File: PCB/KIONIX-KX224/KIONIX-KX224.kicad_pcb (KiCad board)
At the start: 2 copper layers, 4 parts, among them J1 Conn_02x03_Odd_Even

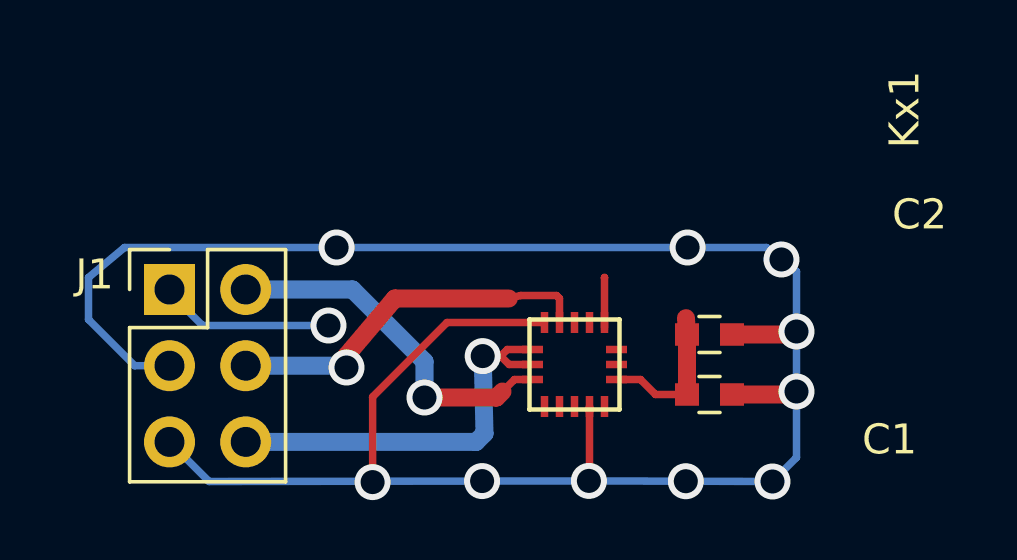
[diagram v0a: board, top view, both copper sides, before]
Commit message: PCB - update KX224
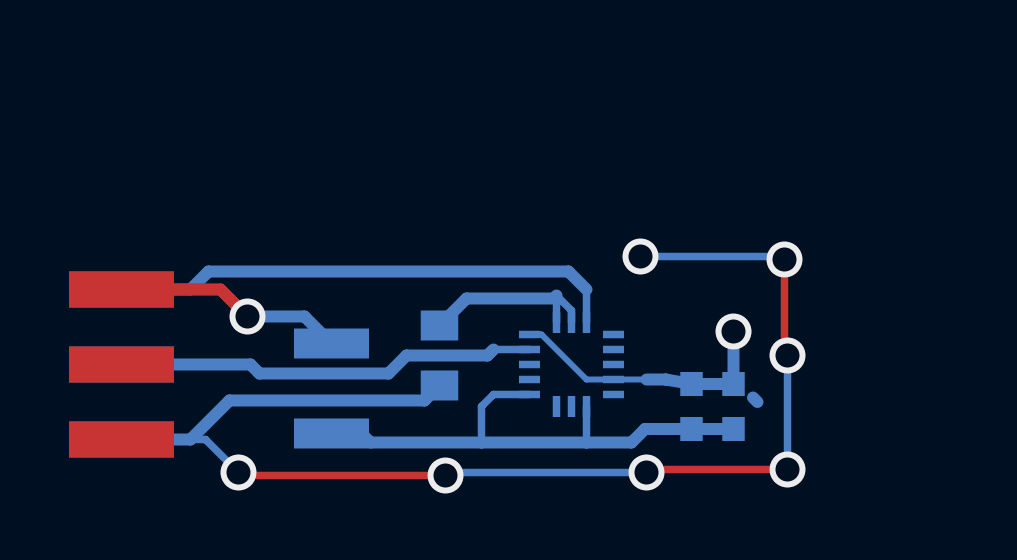
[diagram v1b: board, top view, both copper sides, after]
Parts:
- added J2, J5: Conn_01x01, DIY_KICAD_FOOTPRINT_LIBRARY:pastilles_CMS_rect_1,2_3,5, F.Cu at (128.9, 94.5)
- added J3, J6: Conn_01x01, DIY_KICAD_FOOTPRINT_LIBRARY:pastilles_CMS_rect_1,2_3,5, F.Cu at (128.9, 97.0)
- added J4: Conn_01x01, DIY_KICAD_FOOTPRINT_LIBRARY:pastilles_CMS_rect_1,2_3,5, F.Cu at (128.9, 92.0)
- added JP1: Jumper, Capacitors_SMD:C_0805, B.Cu at (139.5, 94.2)
- added JP2: Jumper, Capacitors_SMD:C_1210, B.Cu at (135.9, 95.3)
- C1, C2, Kx1: moved to B.Cu
- J1: value Conn_02x03_Odd_Even -> Conn_01x01; footprint Pin_Headers:Pin_Header_Straight_2x03_Pitch2.54mm -> DIY_KICAD_FOOTPRINT_LIBRARY:pastilles_CMS_rect_1,2_3,5
- moved C2 2.47 mm to (147.9, 95.9), turned to 90 degrees
- moved J1 1.60 mm to (128.9, 92.0)
- moved C1 0.89 mm to (149.3, 95.9), turned to 90 degrees
- moved Kx1 0.10 mm to (143.9, 94.5), turned to 0 degrees
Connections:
- J1 pad 1: /VDD -> Net-(J1-Pad1)
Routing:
- net GNDREF: track 73.8 -> 9.28 mm, vias 10 -> 1
- net Net-(J6-Pad1): track 0.00 -> 46.1 mm, vias 0 -> 7
- net Net-(J1-Pad1): track 0.00 -> 7.75 mm, vias 0 -> 1
- net /Miso/Mosi: track 13.6 -> 6.38 mm, vias 1 -> 0
- net /CS/SCL: track 12.3 -> 18.6 mm, vias 1 -> 0
- net /VDD: track 12.7 -> 18.6 mm, vias 1 -> 0
- net /SCLK: track 12.6 -> 14.1 mm, vias 1 -> 0

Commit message: PCB - Kionix v 1.5, ready to print
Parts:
- added JP3: Jumper, Capacitors_SMD:C_1210, B.Cu at (140.1, 93.1)
- moved JP1 2.73 mm to (137.0, 95.3)
- moved C1 2.40 mm to (148.8, 93.5), turned to 0 degrees
- moved JP2 2.06 mm to (133.8, 95.5)
- moved C2 1.77 mm to (149.6, 96.5)
- moved Kx1 0.92 mm to (144.5, 95.2)
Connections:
- Kx1 pad 10: (no net) -> Net-(Kx1-Pad10)
- Kx1 pad 11: (no net) -> Net-(Kx1-Pad11)
- Kx1 pad 13: (no net) -> Net-(Kx1-Pad13)
- Kx1 pad 15: (no net) -> Net-(Kx1-Pad15)
- Kx1 pad 16: (no net) -> Net-(Kx1-Pad16)
- Kx1 pad 2: (no net) -> Net-(Kx1-Pad2)
- Kx1 pad 3: (no net) -> Net-(Kx1-Pad3)
- Kx1 pad 5: GNDREF -> Net-(JP3-Pad2)
- Kx1 pad 9: (no net) -> Net-(Kx1-Pad9)
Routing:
- net GNDREF: track 9.28 -> 69.3 mm, vias 1 -> 9
- net Net-(J6-Pad1): track 46.1 -> 8.80 mm, vias 7 -> 0
- net /VDD: track 18.6 -> 25.1 mm
- net Net-(JP3-Pad2): track 0.00 -> 3.19 mm
- net /Miso/Mosi: track 6.38 -> 9.19 mm
- net /SCLK: track 14.1 -> 16.2 mm
- net Net-(J1-Pad1): track 7.75 -> 9.46 mm
- net /CS/SCL: track 18.6 -> 19.6 mm
- added copper zone on B.Cu, net GNDREF
- added copper zone on F.Cu, net GNDREF

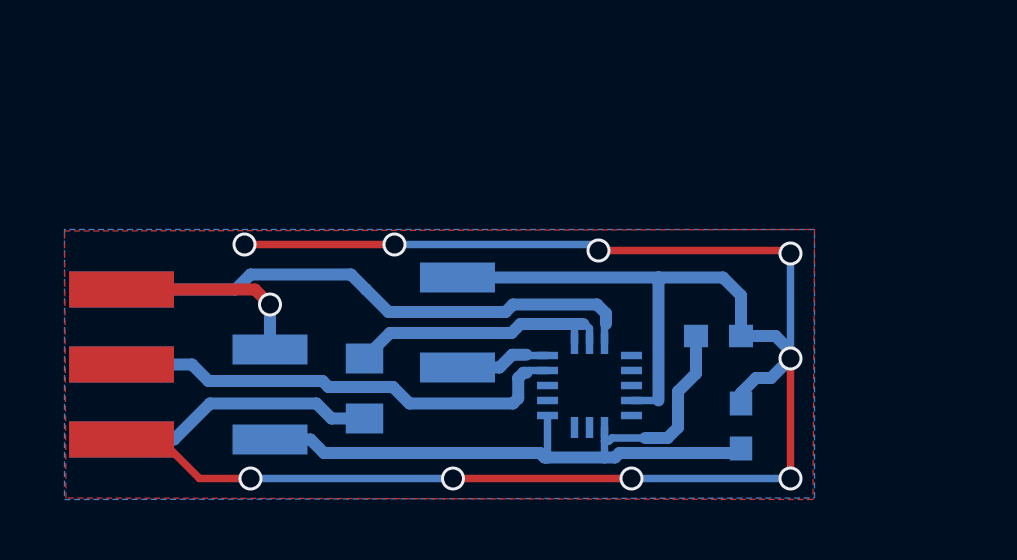
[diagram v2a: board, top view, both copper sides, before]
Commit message: PCB - KX224 update after review with meca staff
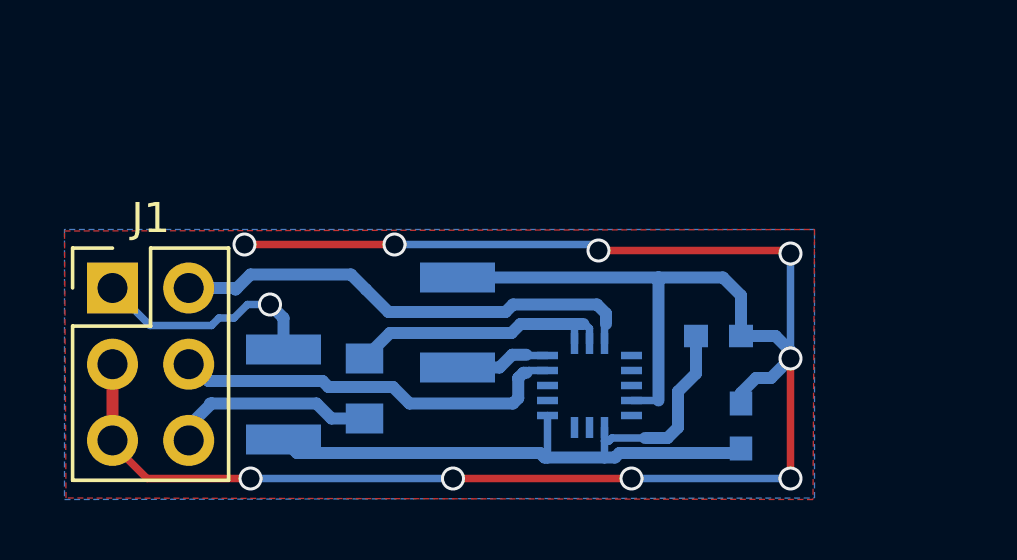
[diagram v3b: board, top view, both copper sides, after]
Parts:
- removed J2, J3, J4, J5, J6: Conn_01x01, DIY_KICAD_FOOTPRINT_LIBRARY:pastilles_CMS_rect_1,2_3,5
- J1: value Conn_01x01 -> Conn_02x03_Odd_Even; footprint DIY_KICAD_FOOTPRINT_LIBRARY:pastilles_CMS_rect_1,2_3,5 -> Pin_Headers:Pin_Header_Straight_2x03_Pitch2.54mm
- moved JP2 0.45 mm to (134.3, 95.5)
- moved J1 0.30 mm to (128.6, 92.0)
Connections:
- JP1 pad 1: Net-(J6-Pad1) -> Net-(J1-Pad6)
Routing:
- net Net-(J6-Pad1): track 8.80 -> 0.00 mm
- net Net-(J1-Pad6): track 0.00 -> 6.90 mm
- net /CS/SCL: track 19.6 -> 16.0 mm
- net GNDREF: track 69.3 -> 72.2 mm
- net /SCLK: track 16.2 -> 13.4 mm
- net Net-(J1-Pad1): track 9.46 -> 7.74 mm

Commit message: PCB - KX224 fix via wiring mistake
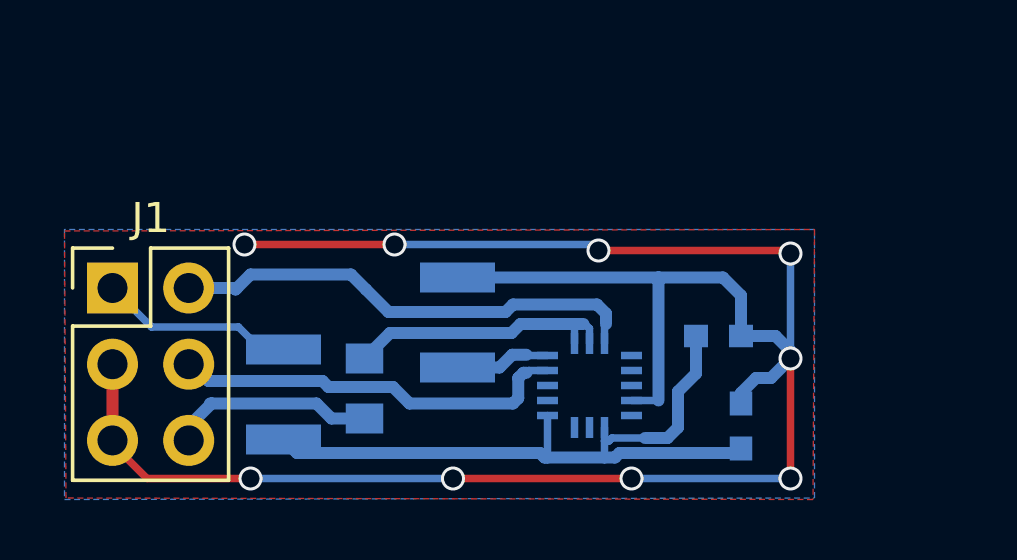
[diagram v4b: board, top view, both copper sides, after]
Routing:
- net Net-(J1-Pad1): track 7.74 -> 6.55 mm, vias 1 -> 0
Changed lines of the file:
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@@
     (thickness 1.6)
     (drawings 6)
-    (tracks 119)
+    (tracks 114)
     (zones 0)
     (modules 7)
@@
   (gr_line (start 127 99) (end 152 99) (angle 90) (layer F.Fab) (width 0.2))
   (gr_line (start 127 90) (end 127 99) (angle 90) (layer F.Fab) (width 0.2))
-  (segment (start 149.55 93.55) (end 150.7 93.55) (width 0.4) (layer B.Cu) (net 1))
-  (segment (start 149.55 95.8) (end 149.55 95.45) (width 0.4) (layer B.Cu) (net 1))
-  (segment (start 149.55 95.45) (end 150.05 94.95) (width 0.4) (layer B.Cu) (net 1))
+  (segment (start 149.55 95.45) (end 150.05 94.95) (width 0.4) (layer B.Cu) (net 1) (status 10))
+  (segment (start 150.55 94.95) (end 151.2 94.3) (width 0.4) (layer B.Cu) (net 1))
   (segment (start 150.05 94.95) (end 150.55 94.95) (width 0.4) (layer B.Cu) (net 1))
+  (segment (start 149.55 95.8) (end 149.55 95.45) (width 0.4) (layer B.Cu) (net 1) (status 30))
+  (segment (start 146.8 95.7) (end 146.8 91.6) (width 0.4) (layer B.Cu) (net 1))
+  (segment (start 145.9 95.7) (end 146.8 95.7) (width 0.25) (layer B.Cu) (net 1) (status 10))
   (segment (start 140.1 91.6) (end 146.8 91.6) (width 0.4) (layer B.Cu) (net 1))
   (segment (start 149.55 92.2) (end 149.55 93.55) (width 0.4) (layer B.Cu) (net 1))
-  (segment (start 146.8 95.7) (end 146.8 91.6) (width 0.4) (layer B.Cu) (net 1))
   (segment (start 146.8 91.6) (end 148.95 91.6) (width 0.4) (layer B.Cu) (net 1))
   (segment (start 148.95 91.6) (end 149.55 92.2) (width 0.4) (layer B.Cu) (net 1))
-  (segment (start 145.9 95.7) (end 146.8 95.7) (width 0.25) (layer B.Cu) (net 1))
-  (segment (start 150.7 93.55) (end 151.2 94.05) (width 0.4) (layer B.Cu) (net 1))
-  (segment (start 150.55 94.95) (end 151.2 94.3) (width 0.4) (layer B.Cu) (net 1))
   (segment (start 128.6 97.03) (end 128.6 94.49) (width 0.4) (layer F.Cu) (net 1))
   (segment (start 133.2 98.3) (end 129.75 98.3) (width 0.25) (layer F.Cu) (net 1))
@@
   (segment (start 129.75 98.3) (end 128.6 97.15) (width 0.25) (layer F.Cu) (net 1))
   (segment (start 128.6 97.15) (end 128.6 97.03) (width 0.25) (layer F.Cu) (net 1))
-  (segment (start 151.2 94.05) (end 151.2 94.3) (width 0.4) (layer B.Cu) (net 1))
   (segment (start 151.2 94.3) (end 151.2 90.8) (width 0.25) (layer B.Cu) (net 1))
   (via (at 133 90.5) (size 0.8) (drill 0.6) (layers F.Cu B.Cu) (net 1))
@@
   (segment (start 151.2 90.8) (end 151.1 90.7) (width 0.25) (layer F.Cu) (net 1))
   (via (at 151.2 90.8) (size 0.8) (drill 0.6) (layers F.Cu B.Cu) (net 1))
-  (segment (start 134.75 97.45) (end 142.6 97.45) (width 0.4) (layer B.Cu) (net 2))
-  (segment (start 142.85 97.45) (end 143 97.6) (width 0.4) (layer B.Cu) (net 2))
-  (segment (start 143 97.6) (end 143.1 97.6) (width 0.4) (layer B.Cu) (net 2))
-  (segment (start 142.6 97.45) (end 142.85 97.45) (width 0.4) (layer B.Cu) (net 2))
-  (segment (start 134.75 97.45) (end 134.3 97) (width 0.4) (layer B.Cu) (net 2))
-  (segment (start 149.4 97.45) (end 148 97.45) (width 0.4) (layer B.Cu) (net 2))
+  (segment (start 150.7 93.55) (end 151.2 94.05) (width 0.4) (layer B.Cu) (net 1))
+  (segment (start 151.2 94.05) (end 151.2 94.3) (width 0.4) (layer B.Cu) (net 1))
+  (segment (start 149.55 93.55) (end 150.7 93.55) (width 0.4) (layer B.Cu) (net 1))
+  (segment (start 149.4 97.45) (end 148 97.45) (width 0.4) (layer B.Cu) (net 2) (status 10))
   (segment (start 145.5 97.45) (end 148 97.45) (width 0.4) (layer B.Cu) (net 2))
   (segment (start 145.35 97.6) (end 145.5 97.45) (width 0.4) (layer B.Cu) (net 2))
   (segment (start 145.35 97.6) (end 145 97.6) (width 0.4) (layer B.Cu) (net 2))
-  (segment (start 149.4 97.45) (end 149.55 97.3) (width 0.4) (layer B.Cu) (net 2))
+  (segment (start 149.4 97.45) (end 149.55 97.3) (width 0.4) (layer B.Cu) (net 2) (status 30))
   (segment (start 148.05 94.8) (end 147.45 95.4) (width 0.4) (layer B.Cu) (net 2))
   (segment (start 147.45 95.4) (end 147.45 96.6) (width 0.4) (layer B.Cu) (net 2))
@@
   (segment (start 148.05 94.8) (end 148.05 93.55) (width 0.4) (layer B.Cu) (net 2))
   (segment (start 145.25 96.95) (end 146.35 96.95) (width 0.25) (layer B.Cu) (net 2))
+  (segment (start 145 97.05) (end 145.15 97.05) (width 0.25) (layer B.Cu) (net 2))
+  (segment (start 145.15 97.05) (end 145.25 96.95) (width 0.25) (layer B.Cu) (net 2))
+  (segment (start 148.2 93.7) (end 148.05 93.55) (width 0.25) (layer B.Cu) (net 2))
   (segment (start 145 97.05) (end 145 97.6) (width 0.25) (layer B.Cu) (net 2))
+  (segment (start 145 96.6) (end 145 97.05) (width 0.25) (layer B.Cu) (net 2) (status 10))
   (segment (start 145 97.6) (end 145 97.5) (width 0.25) (layer B.Cu) (net 2))
+  (segment (start 143.1 97.6) (end 145 97.6) (width 0.4) (layer B.Cu) (net 2))
   (segment (start 145 97.5) (end 145 97.6) (width 0.25) (layer B.Cu) (net 2))
-  (segment (start 143.1 96.2) (end 143.1 97.6) (width 0.25) (layer B.Cu) (net 2))
+  (segment (start 143.1 96.2) (end 143.1 97.6) (width 0.25) (layer B.Cu) (net 2) (status 10))
   (segment (start 143.1 97.6) (end 143.1 97.45) (width 0.25) (layer B.Cu) (net 2))
   (segment (start 143.1 97.45) (end 143.1 97.6) (width 0.25) (layer B.Cu) (net 2))
-  (segment (start 143.1 97.6) (end 145 97.6) (width 0.4) (layer B.Cu) (net 2))
-  (segment (start 148.2 93.7) (end 148.05 93.55) (width 0.25) (layer B.Cu) (net 2))
-  (segment (start 145 97.05) (end 145.15 97.05) (width 0.25) (layer B.Cu) (net 2))
-  (segment (start 145.15 97.05) (end 145.25 96.95) (width 0.25) (layer B.Cu) (net 2))
-  (segment (start 145 96.6) (end 145 97.05) (width 0.25) (layer B.Cu) (net 2))
+  (segment (start 134.75 97.45) (end 142.6 97.45) (width 0.4) (layer B.Cu) (net 2))
+  (segment (start 142.6 97.45) (end 142.85 97.45) (width 0.4) (layer B.Cu) (net 2))
+  (segment (start 143 97.6) (end 143.1 97.6) (width 0.4) (layer B.Cu) (net 2))
+  (segment (start 142.85 97.45) (end 143 97.6) (width 0.4) (layer B.Cu) (net 2))
+  (segment (start 134.75 97.45) (end 134.3 97) (width 0.4) (layer B.Cu) (net 2))
   (segment (start 131.14 91.95) (end 132.75 91.95) (width 0.4) (layer B.Cu) (net 3))
   (segment (start 132.7 92) (end 133.2 91.5) (width 0.4) (layer B.Cu) (net 3))
   (segment (start 133.2 91.5) (end 136.55 91.5) (width 0.4) (layer B.Cu) (net 3))
   (segment (start 136.55 91.5) (end 137.05 92) (width 0.4) (layer B.Cu) (net 3))
-  (segment (start 145 93.2) (end 145 93.8) (width 0.25) (layer B.Cu) (net 3))
+  (segment (start 145 93.2) (end 145 93.8) (width 0.25) (layer B.Cu) (net 3) (status 20))
   (segment (start 145 93.2) (end 145.05 93.15) (width 0.25) (layer B.Cu) (net 3))
   (segment (start 137.05 92) (end 137.8 92.75) (width 0.4) (layer B.Cu) (net 3))
@@
   (segment (start 131.14 94.49) (end 131.24 94.49) (width 0.4) (layer B.Cu) (net 4))
   (segment (start 131.24 94.49) (end 131.8 95.05) (width 0.4) (layer B.Cu) (net 4))
-  (segment (start 143.1 94.7) (end 142.475 94.7) (width 0.25) (layer B.Cu) (net 4))
+  (segment (start 143.1 94.7) (end 142.475 94.7) (width 0.25) (layer B.Cu) (net 4) (status 10))
   (segment (start 138.5 95.8) (end 137.95 95.25) (width 0.4) (layer B.Cu) (net 4))
   (segment (start 137.95 95.25) (end 135.8 95.25) (width 0.4) (layer B.Cu) (net 4))
@@
   (segment (start 142.2 93.15) (end 141.9 93.45) (width 0.4) (layer B.Cu) (net 5))
   (segment (start 144 93.15) (end 142.2 93.15) (width 0.4) (layer B.Cu) (net 5))
-  (segment (start 144.5 93.8) (end 144.5 93.3) (width 0.25) (layer B.Cu) (net 5))
+  (segment (start 144.5 93.8) (end 144.5 93.3) (width 0.25) (layer B.Cu) (net 5) (status 10))
   (segment (start 144.3 93.15) (end 144 93.15) (width 0.4) (layer B.Cu) (net 5))
   (segment (start 144.35 93.15) (end 144.3 93.15) (width 0.25) (layer B.Cu) (net 5))
   (segment (start 144.5 93.3) (end 144.35 93.15) (width 0.25) (layer B.Cu) (net 5))
-  (segment (start 144 93.15) (end 144 93.8) (width 0.25) (layer B.Cu) (net 5))
-  (segment (start 133.85 92.5) (end 134.3 92.95) (width 0.4) (layer B.Cu) (net 6))
-  (segment (start 133.1 92.5) (end 132.65 92.95) (width 0.25) (layer B.Cu) (net 6))
-  (segment (start 132.65 92.95) (end 132.15 92.95) (width 0.25) (layer B.Cu) (net 6))
-  (segment (start 132.15 92.95) (end 131.9 93.2) (width 0.25) (layer B.Cu) (net 6))
-  (segment (start 131.9 93.2) (end 129.85 93.2) (width 0.25) (layer B.Cu) (net 6))
-  (segment (start 128.6 91.95) (end 129.85 93.2) (width 0.25) (layer B.Cu) (net 6))
-  (via (at 133.85 92.5) (size 0.8) (drill 0.6) (layers F.Cu B.Cu) (net 6))
-  (segment (start 133.85 92.5) (end 133.1 92.5) (width 0.25) (layer B.Cu) (net 6))
-  (segment (start 134.3 92.95) (end 134.3 94) (width 0.4) (layer B.Cu) (net 6))
-  (segment (start 143.1 94.2) (end 142.425002 94.2) (width 0.25) (layer B.Cu) (net 7))
+  (segment (start 144 93.15) (end 144 93.8) (width 0.25) (layer B.Cu) (net 5) (status 20))
+  (segment (start 128.6 91.95) (end 129.9 93.25) (width 0.25) (layer B.Cu) (net 6) (status 400000))
+  (segment (start 132.8 93.25) (end 133.55 94) (width 0.25) (layer B.Cu) (net 6) (status 800000))
+  (segment (start 129.9 93.25) (end 132.8 93.25) (width 0.25) (layer B.Cu) (net 6))
+  (segment (start 133.55 94) (end 134.3 94) (width 0.25) (layer B.Cu) (net 6) (status C00000))
+  (segment (start 143.1 94.2) (end 142.425002 94.2) (width 0.25) (layer B.Cu) (net 7) (status 10))
   (segment (start 141.5 94.6) (end 141.925002 94.174998) (width 0.4) (layer B.Cu) (net 7))
   (segment (start 141.925002 94.174998) (end 142.4 94.174998) (width 0.4) (layer B.Cu) (net 7))
@@
     (connect_pads (clearance 0.508))
     (min_thickness 0.254)
-    (fill yes (arc_segments 16) (thermal_gap 0.508) (thermal_bridge_width 0.508))
+    (fill (arc_segments 16) (thermal_gap 0.508) (thermal_bridge_width 0.508))
     (polygon
       (pts
@@
     (connect_pads (clearance 0.508))
     (min_thickness 0.254)
-    (fill yes (arc_segments 16) (thermal_gap 0.508) (thermal_bridge_width 0.508))
+    (fill (arc_segments 16) (thermal_gap 0.508) (thermal_bridge_width 0.508))
     (polygon
       (pts
